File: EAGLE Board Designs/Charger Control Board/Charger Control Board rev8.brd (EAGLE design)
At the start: 86.4 x 83.8 mm, 121 parts, among them K1 RELAY_DPDT_RT424024, K2 RELAY_DPDT_RT424024, K3 RELAY_DPDT_RT424024, U1 LOGICGATE_BUFFER, U2 ADM8316WBX30, U3 VOLTAGE_REGULATOR_MODULE_OKI-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, U4 TCAN1051HQV-Q1, U5 TCAN1051HQV-Q1

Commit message: changed AUX CAN connector
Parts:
- removed AUX_CAN: CONNECTOR-CAN_MF_T_V_, HyTechDevices - Copy:MOLEX_MICROFIT_PTH_VERTICAL_04_DUAL
- added J1: CONNECTOR-4_μF_T_V_BLACK, HyTechDevices:MOLEX_MICROFIT_PTH_VERTICAL_04_DUAL
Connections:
- net +12V: now also J1.1; no longer AUX_CAN.1
- net CANH: now also J1.2; no longer AUX_CAN.4
- net CANL: now also J1.3; no longer AUX_CAN.3
- net GND: now also J1.4; no longer AUX_CAN.2
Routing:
- net CANH: track 147.0 -> 137.0 mm
- net CANL: track 158.3 -> 150.1 mm
- net +12V: track 138.2 -> 136.0 mm
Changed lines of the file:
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@@
 <attribute name="VOLTAGE" value="10V" x="11.684" y="35.306" size="1.778" layer="27" display="off"/>
-</element>
-<element name="AUX_CAN" library="HyTechDevices - Copy" package="MOLEX_MICROFIT_PTH_VERTICAL_04_DUAL" value="CONNECTOR-CAN_MF_T_V_" x="12.7" y="4.826" smashed="yes" rot="R180">
-<attribute name="MANUFACTURER" value="Molex" x="19.05" y="-7.874" size="1.778" layer="27" rot="R180" display="off"/>
-<attribute name="MPN" value="430450414" x="19.05" y="-7.874" size="1.778" layer="27" rot="R180" display="off"/>
-<attribute name="NAME" x="7.62" y="6.858" size="0.8128" layer="25" font="vector" rot="R90" align="bottom-center"/>
 </element>
 <element name="POWER" library="HyTechDevices" package="MOLEX_MICROFIT_PTH_VERTICAL_02_DUAL" value="CONNECTOR-2_μF_T_V_" x="3.937" y="15.875" smashed="yes" rot="R90">
@@
 <attribute name="MPN" value="TCAN1051HGVDRQ1" x="2.54" y="-13.97" size="1.778" layer="27" display="off"/>
 <attribute name="NAME" x="-0.635" y="-13.97" size="0.8128" layer="25" font="vector" rot="R90" align="bottom-center"/>
+</element>
+<element name="J1" library="HyTechDevices" package="MOLEX_MICROFIT_PTH_VERTICAL_04_DUAL" value="CONNECTOR-4_μF_T_V_BLACK" x="-8.89" y="-8.89" smashed="yes">
+<attribute name="DKPN" value="2266-43045-0414-ND" x="-8.89" y="-8.89" size="1.778" layer="27" display="off"/>
+<attribute name="MANUFACTURER" value="Molex" x="-8.89" y="-8.89" size="1.778" layer="27" display="off"/>
+<attribute name="MOPN" value="538-43045-0414" x="-8.89" y="-8.89" size="1.778" layer="27" display="off"/>
+<attribute name="MPN" value="430450414" x="-8.89" y="-8.89" size="1.778" layer="27" display="off"/>
+<attribute name="NAME" x="-8.89" y="-15.367" size="0.8128" layer="25" rot="R180" align="bottom-center"/>
 </element>
 </elements>
@@
 <contactref element="C4" pad="1"/>
 <contactref element="C5" pad="2"/>
-<contactref element="AUX_CAN" pad="2"/>
 <contactref element="POWER" pad="2"/>
 <contactref element="C3" pad="1"/>
@@
 <contactref element="U5" pad="8"/>
 <contactref element="U4" pad="8"/>
+<contactref element="J1" pad="4"/>
 <wire x1="78.6774" y1="53.4416" x2="81.5594" y2="53.34" width="0" layer="19" extent="1-1"/>
 <wire x1="76.708" y1="56.388" x2="76.835" y2="53.4416" width="0" layer="19" extent="1-1"/>
@@
 <wire x1="5.7658" y1="6.4438" x2="2.7686" y2="7.0104" width="0" layer="19" extent="16-16"/>
 <wire x1="11.3284" y1="12.9152" x2="3.937" y2="15.875" width="0" layer="19" extent="1-1"/>
-<wire x1="14.1986" y1="7.8232" x2="12.4042875" y2="11.8962875" width="0" layer="19" extent="1-1"/>
 <wire x1="48.9204" y1="48.6918" x2="52.8442" y2="57.277" width="0" layer="19" extent="1-1"/>
 <wire x1="0.635" y1="-3.7465" x2="2.7686" y2="7.0104" width="0" layer="19" extent="1-1"/>
@@
 <wire x1="0.635" y1="-11.3665" x2="1.905" y2="-8.9535" width="0" layer="19" extent="1-1"/>
 <wire x1="1.905" y1="-16.5735" x2="0.635" y2="-11.3665" width="0" layer="19" extent="1-1"/>
-<wire x1="24.4602" y1="13.5763" x2="14.1986" y2="7.8232" width="0" layer="19" extent="16-16"/>
+<wire x1="-10.3886" y1="-8.89" x2="0.635" y2="-11.3665" width="0" layer="19" extent="1-1"/>
+<wire x1="24.4602" y1="13.5763" x2="18.669" y2="24.257" width="0" layer="19" extent="1-16"/>
 <wire x1="28.2702" y1="13.5763" x2="24.4602" y2="13.5763" width="0" layer="19" extent="16-16"/>
 <wire x1="28.8036" y1="7.8232" x2="28.2702" y2="13.5763" width="0" layer="19" extent="16-16"/>
@@
 <contactref element="C7" pad="1"/>
 <contactref element="MAIN_CONNECTOR" pad="4"/>
-<contactref element="AUX_CAN" pad="1"/>
 <contactref element="XF1" pad="4"/>
 <contactref element="XF1" pad="3"/>
@@
 <wire x1="14.492" y1="24.0544" x2="13.9806" y2="23.368" width="0.381" layer="1"/>
 <wire x1="12.8016" y1="0.889" x2="9.652" y2="4.0386" width="0.762" layer="1"/>
-<wire x1="11.2014" y1="7.8232" x2="9.652" y2="6.2738" width="0.762" layer="1"/>
 <wire x1="9.652" y1="6.2738" x2="9.652" y2="4.0386" width="0.762" layer="1"/>
 <wire x1="33.3248" y1="3.6668" x2="30.547" y2="0.889" width="0.762" layer="1"/>
@@
 <wire x1="40.0402" y1="32.8676" x2="39.9386" y2="32.766" width="0.381" layer="1"/>
 <wire x1="39.9386" y1="32.766" x2="37.465" y2="32.766" width="0.381" layer="1"/>
+<contactref element="J1" pad="1"/>
+<wire x1="9.652" y1="6.2738" x2="-7.3914" y2="-11.8872" width="0" layer="19" extent="1-1"/>
 </signal>
 <signal name="+5V">
@@
 <contactref element="D100" pad="2"/>
 <contactref element="R40" pad="1"/>
-<contactref element="AUX_CAN" pad="3"/>
 <contactref element="CHG_CAN" pad="5"/>
 <wire x1="25.8064" y1="7.8232" x2="25.8064" y2="6.8072" width="0.254" layer="16"/>
@@
 <wire x1="25.6336" y1="0.9756" x2="28.214" y2="3.556" width="0.254" layer="16"/>
 <wire x1="28.214" y1="3.556" x2="33.42503125" y2="3.556" width="0.254" layer="16"/>
-<wire x1="12.7254" y1="6.35" x2="11.2014" y2="4.826" width="0.254" layer="1"/>
 <wire x1="13.2334" y1="12.8152" x2="14.3646" y2="11.684" width="0.254" layer="1"/>
 <wire x1="14.3646" y1="11.684" x2="15.748" y2="11.684" width="0.254" layer="1"/>
@@
 <wire x1="11.2014" y1="5.3822" x2="7.9398" y2="8.6438" width="0.254" layer="16"/>
 <wire x1="6.4158" y1="8.6438" x2="7.9398" y2="8.6438" width="0.254" layer="16"/>
-<wire x1="11.2014" y1="4.826" x2="11.2014" y2="5.3822" width="0.254" layer="16"/>
-<wire x1="11.2014" y1="4.826" x2="15.0518" y2="0.9756" width="0.254" layer="16"/>
 <wire x1="15.0518" y1="0.9756" x2="24.2316" y2="0.9756" width="0.254" layer="16"/>
 <wire x1="24.2316" y1="0.9756" x2="25.6336" y2="0.9756" width="0.254" layer="16"/>
@@
 <contactref element="U4" pad="6"/>
 <contactref element="U5" pad="6"/>
-<wire x1="3.175" y1="-3.7465" x2="11.2014" y2="4.826" width="0" layer="19" extent="1-1"/>
+<contactref element="J1" pad="3"/>
+<wire x1="12.7254" y1="6.35" x2="11.2014" y2="5.3822" width="0" layer="19" extent="1-16"/>
+<wire x1="15.0518" y1="0.9756" x2="11.2014" y2="5.3822" width="0" layer="19" extent="16-16"/>
+<wire x1="3.175" y1="-3.7465" x2="11.2014" y2="5.3822" width="0" layer="19" extent="1-16"/>
 <wire x1="3.175" y1="-11.3665" x2="3.175" y2="-3.7465" width="0" layer="19" extent="1-1"/>
+<wire x1="-7.3914" y1="-8.89" x2="3.175" y2="-11.3665" width="0" layer="19" extent="1-1"/>
 </signal>
 <signal name="CANH">
 <contactref element="MAIN_CONNECTOR" pad="1"/>
 <contactref element="D100" pad="1"/>
-<contactref element="AUX_CAN" pad="4"/>
 <contactref element="CHG_CAN" pad="4"/>
 <wire x1="40.0558" y1="4.826" x2="32.1818" y2="12.7" width="0.254" layer="16"/>
@@
 <wire x1="22.8092" y1="7.8232" x2="18.2118" y2="7.8232" width="0.254" layer="16"/>
 <wire x1="18.2118" y1="7.8232" x2="15.2146" y2="4.826" width="0.254" layer="16"/>
-<wire x1="15.2146" y1="4.826" x2="14.1986" y2="4.826" width="0.254" layer="16"/>
-<wire x1="14.1986" y1="4.826" x2="12.6746" y2="6.35" width="0.254" layer="16"/>
 <wire x1="12.6746" y1="8.382" x2="12.6746" y2="6.35" width="0.254" layer="16"/>
 <wire x1="12.6746" y1="8.382" x2="11.6586" y2="9.398" width="0.254" layer="16"/>
@@
 <wire x1="11.176" y1="54.356" x2="16.8275" y2="54.356" width="0.254" layer="16"/>
 <contactref element="CAN_TERM" pad="2"/>
-<wire x1="14.1986" y1="4.826" x2="19.05" y2="9.6774" width="0.254" layer="1"/>
 <wire x1="19.05" y1="13.8176" x2="19.05" y2="9.6774" width="0.254" layer="1"/>
 <wire x1="5.08" y1="9.398" x2="5.1158" y2="9.3622" width="0.254" layer="16"/>
@@
 <contactref element="U4" pad="7"/>
 <contactref element="U5" pad="7"/>
+<contactref element="J1" pad="2"/>
+<wire x1="22.8092" y1="7.8232" x2="19.05" y2="9.6774" width="0" layer="19" extent="1-1"/>
+<wire x1="12.6746" y1="6.35" x2="15.2146" y2="4.826" width="0" layer="19" extent="16-16"/>
 <wire x1="1.905" y1="-3.7465" x2="5.1158" y2="8.6438" width="0" layer="19" extent="1-16"/>
 <wire x1="1.905" y1="-11.3665" x2="1.905" y2="-3.7465" width="0" layer="19" extent="1-1"/>
+<wire x1="-10.3886" y1="-11.8872" x2="1.905" y2="-11.3665" width="0" layer="19" extent="1-1"/>
 </signal>
 <signal name="+3V3">

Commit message: replaced R3,R4,R5,R6 resistors
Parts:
- R3, R4, R5, R6: value RESISTOR_0603_1K -> RESISTOR_0603_2K

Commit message: update resistors for LEDs
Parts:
- R1, R26, R7, R8: value RESISTOR_0603_1K -> RESISTOR_0603_2.18K
- R2, R9: value RESISTOR_0603_1K -> RESISTOR_0603_2K

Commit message: updated voltage dividers
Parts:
- R11, R12, R13, R14, R15, R16: value RESISTOR_0603_12K -> RESISTOR_0603_5.1K

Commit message: small changes
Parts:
- D101, D102: value TVS_15V -> TVS_30VDO-214AA; device HyTechDevices:SOT-23 -> HyTechDevices:DO-214AA
- R1, R26, R7, R8: value RESISTOR_0603_2.18K -> RESISTOR_0603_2K
- R100: value RESISTOR_0603_240 -> RESISTOR_0603_5.9K; device HyTechDevices_Jumper:0603-RES -> HyTechDevices:0603-RES
- R31: value RESISTOR_0603_240 -> RESISTOR_0603_470
- R38: value RESISTOR_0603_1K -> RESISTOR_0603_2K
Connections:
- net BMS_OK: now also D101.2; no longer D101.3
- net IMD_OK: now also D102.2; no longer D102.3
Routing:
- net IMD_OK: track 115.4 -> 117.6 mm
- net BMS_OK: track 97.3 -> 99.5 mm

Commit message: checked there is no more 12V
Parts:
- R10: value RESISTOR_0603_12K -> RESISTOR_0603_5.1K
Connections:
- net +12V renamed +24V
- net 12V_READ renamed 24V_READ
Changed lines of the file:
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@@
 <attribute name="VOLTAGE_MAX" value="350V" x="21.082" y="59.055" size="1.778" layer="27" rot="R180" display="off"/>
 </element>
-<element name="R10" library="HyTechDevices" package="0603-RES" value="RESISTOR_0603_12K" x="22.352" y="57.15" smashed="yes">
-<attribute name="DKPN" value="311-12.0KHRCT-ND" x="23.622" y="53.34" size="1.778" layer="27" display="off"/>
+<element name="R10" library="HyTechDevices" package="0603-RES" value="RESISTOR_0603_5.1K" x="22.352" y="57.15" smashed="yes">
+<attribute name="DKPN" value="311-5.10KHRTR-ND" x="23.622" y="53.34" size="1.778" layer="27" display="off"/>
 <attribute name="MANUFACTURER" value="Yageo" x="23.622" y="53.34" size="1.778" layer="27" display="off"/>
-<attribute name="MOPN" value="603-RC0603FR-0712KL" x="23.622" y="53.34" size="1.778" layer="27" display="off"/>
-<attribute name="MPN" value="RC0603FR-0712KL" x="23.622" y="53.34" size="1.778" layer="27" display="off"/>
+<attribute name="MOPN" value="603-RC0603FR-075K1L " x="23.622" y="53.34" size="1.778" layer="27" display="off"/>
+<attribute name="MPN" value="RC0603FR-075K1L" x="23.622" y="53.34" size="1.778" layer="27" display="off"/>
 <attribute name="NAME" x="22.352" y="57.785" size="0.8128" layer="25" font="vector" align="bottom-center"/>
 <attribute name="POWER" value="0.1W" x="23.622" y="53.34" size="1.778" layer="27" display="off"/>
-<attribute name="RESISTANCE" value="12k" x="23.622" y="53.34" size="1.778" layer="27" display="off"/>
+<attribute name="RESISTANCE" value="5.1k" x="23.622" y="53.34" size="1.778" layer="27" display="off"/>
 <attribute name="TOLERANCE" value="1%" x="23.622" y="53.34" size="1.778" layer="27" display="off"/>
-<attribute name="VOLTAGE_CONTINUOUS" value="34.64V" x="23.622" y="53.34" size="1.778" layer="27" display="off"/>
+<attribute name="VOLTAGE_CONTINUOUS" value="22.58V" x="23.622" y="53.34" size="1.778" layer="27" display="off"/>
 <attribute name="VOLTAGE_MAX" value="75V" x="23.622" y="53.34" size="1.778" layer="27" display="off"/>
 </element>
@@
 <wire x1="4.9784" y1="13.9192" x2="6.9342" y2="15.875" width="0.254" layer="1"/>
 </signal>
-<signal name="+12V">
+<signal name="+24V">
 <contactref element="U3" pad="1"/>
 <contactref element="C7" pad="1"/>
@@
 <wire x1="32.9946" y1="62.2046" x2="32.9946" y2="80.0354" width="0.254" layer="1"/>
 </signal>
-<signal name="12V_READ">
+<signal name="24V_READ">
 <contactref element="R17" pad="2"/>
 <contactref element="R10" pad="1"/>

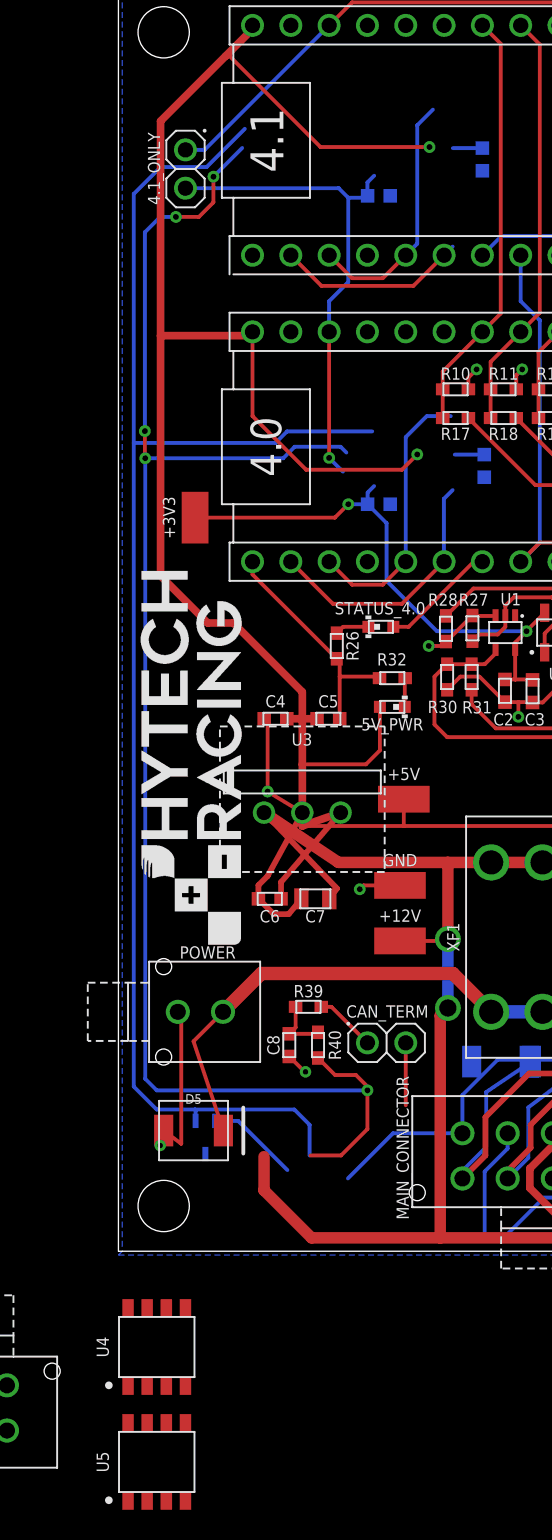
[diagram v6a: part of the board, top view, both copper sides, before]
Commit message: positioning of U4, U5
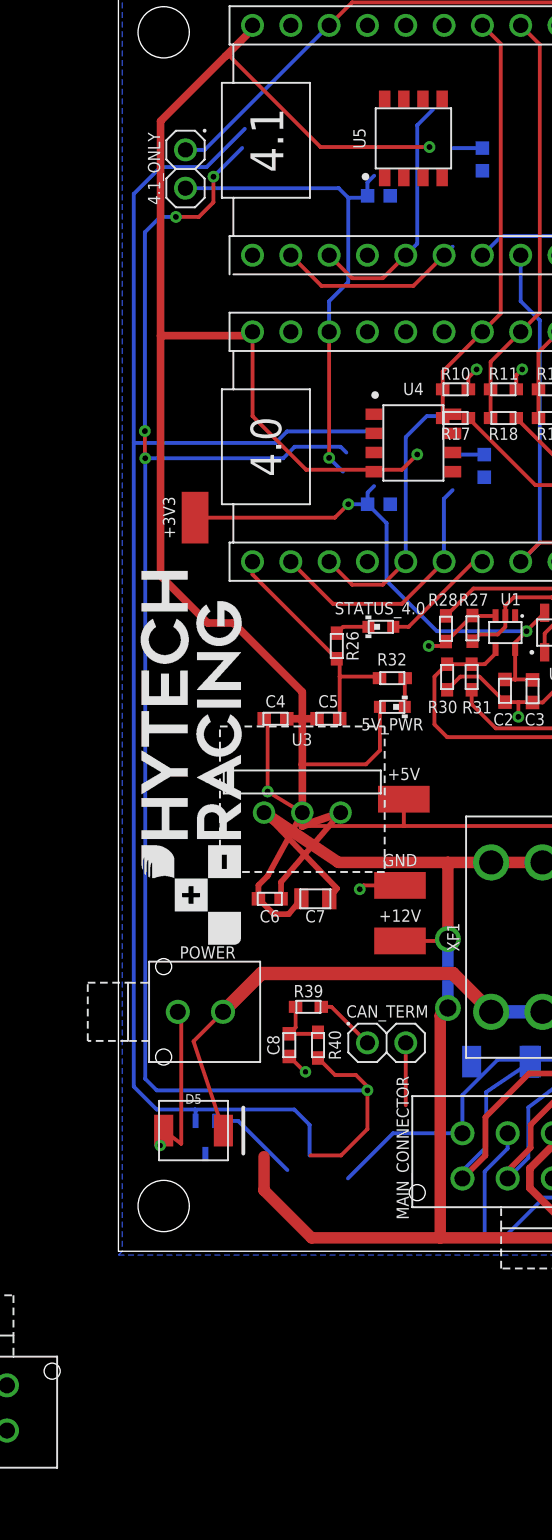
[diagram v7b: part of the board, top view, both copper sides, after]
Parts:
- moved U5 89.4 mm to (19.6, 73.8)
- moved U4 62.3 mm to (19.6, 53.6), turned to 270 degrees
